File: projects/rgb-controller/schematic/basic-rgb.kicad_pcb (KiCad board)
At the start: 2 copper layers, 49.5 x 37.2 mm, 11 parts, among them J1 PLAYPAD, J2 FTDI, J3 USB_DBG, J4 USB_C_Receptacle_PowerOnly_6P, U1 XIAO-ESP32-S3-SMD

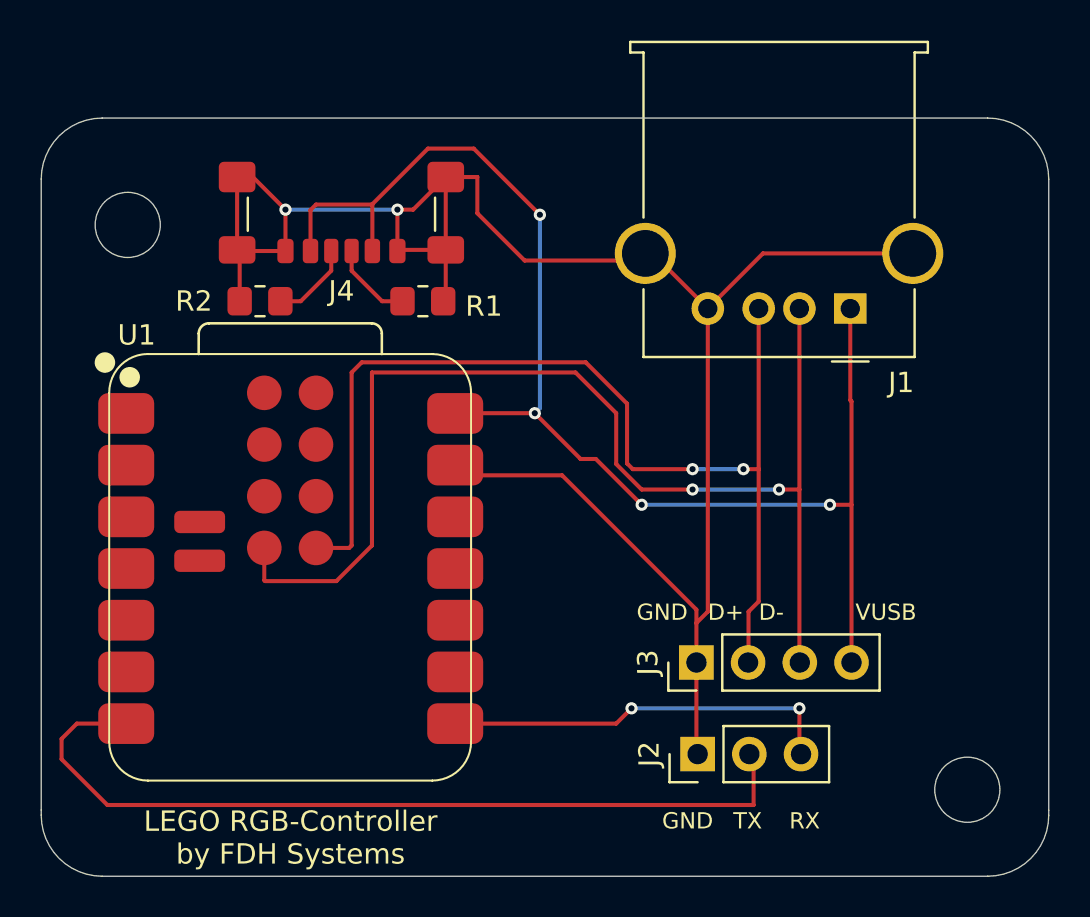
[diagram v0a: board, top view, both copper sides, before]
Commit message: feat: add xbox 360 support + extra emulator tweaks
Adds Xbox 360 Support into the RGB-Controller project, tweaks fronend UI design for emulator, as well as adding a case for the RGB-Controller + Redesigning the PCB for RGB-controller

BREAKING CHANGE:
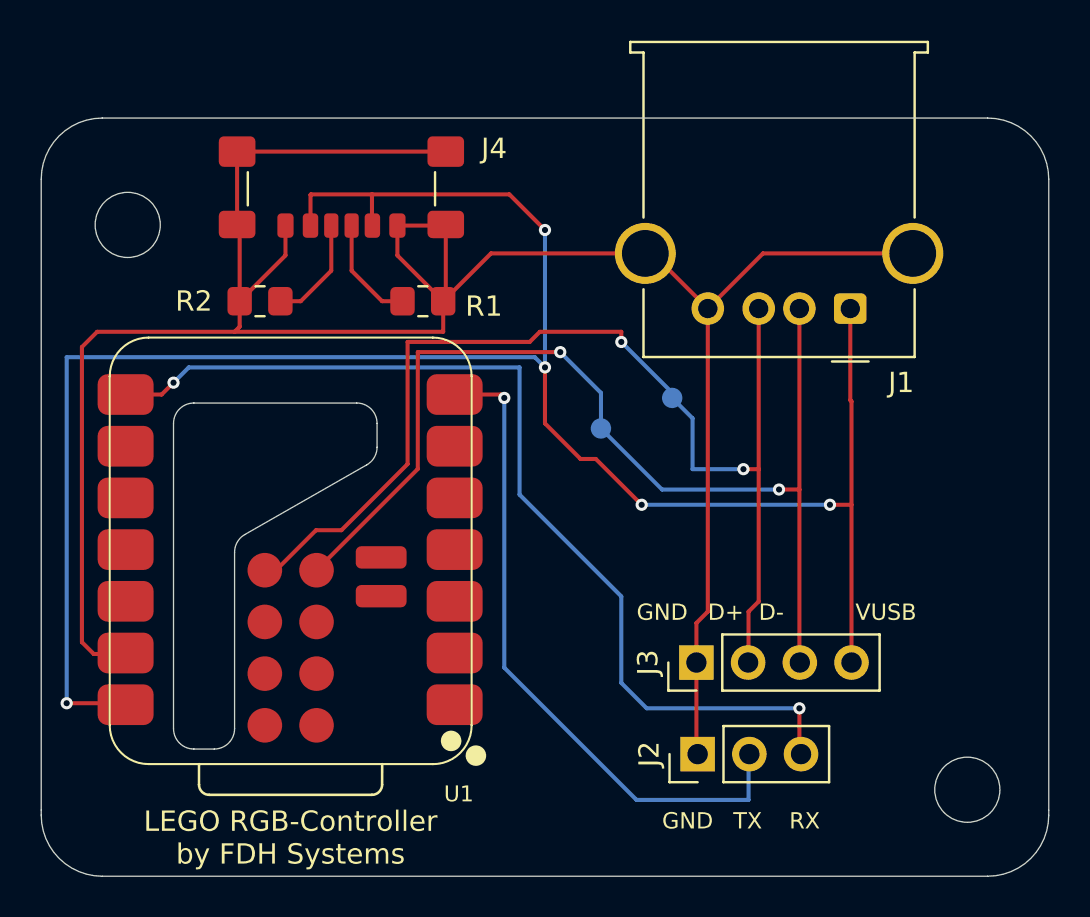
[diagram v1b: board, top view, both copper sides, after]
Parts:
- added REF**: TestPoint_Pad_D1.0mm, TestPoint:TestPoint_Pad_D1.0mm, B.Cu at (133.0, 85.0)
- added REF**: TestPoint_Pad_D1.0mm, TestPoint:TestPoint_Pad_D1.0mm, B.Cu at (136.5, 83.5)
- moved G*** 31.4 mm to (149.8, 85.0)
- moved G*** 16.8 mm to (122.5, 101.2)
- moved J4 1.25 mm to (120.2, 72.0)
- moved U1 0.84 mm to (117.8, 91.0), turned to 180 degrees
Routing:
- net +5V: track 67.8 -> 102.7 mm, vias 4 -> 5
- net Net-(J2-Pin_3): track 19.5 -> 49.0 mm
- net GND: track 98.4 -> 120.6 mm, vias 2 -> 0
- net Net-(J2-Pin_2): track 41.9 -> 32.7 mm, vias 0 -> 1
- net Net-(J1-D-): track 58.4 -> 52.4 mm
- net Net-(J1-D+): track 52.0 -> 54.9 mm
- net Net-(J4-CC2): track 4.09 -> 5.34 mm
- net Net-(J4-CC1): track 4.09 -> 5.34 mm
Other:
- outline, holes or cut-outs redrawn
